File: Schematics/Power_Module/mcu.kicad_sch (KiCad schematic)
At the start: 38 parts, among them J5 USB_C_Female_USB2_Small, J6 SWD_B, J7 Stack Male Edge Connector, SW1 SW_STM_RESET, SW2 SW_STM_BOOT_MODE, U13 CP2102N-A02-GQFN20R, U14 STM32F103CBT6, U15 ISO1044BDR, U16 W25Q128JVS, Y1 X322516MMB4SI

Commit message: confirm layout, confirm everything fits
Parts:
- added C49: 22uF, symbol Device:C
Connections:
- net +3V3 is gone; now on net 3.3V_MUX: C46.1, U15.1 (VCC1)
- net +5V is gone; now on net 5.0V_A: C47.1, U15.8 (VCC2)
- net 24V_MUX: now also C49.1
- net GND: now also C49.2

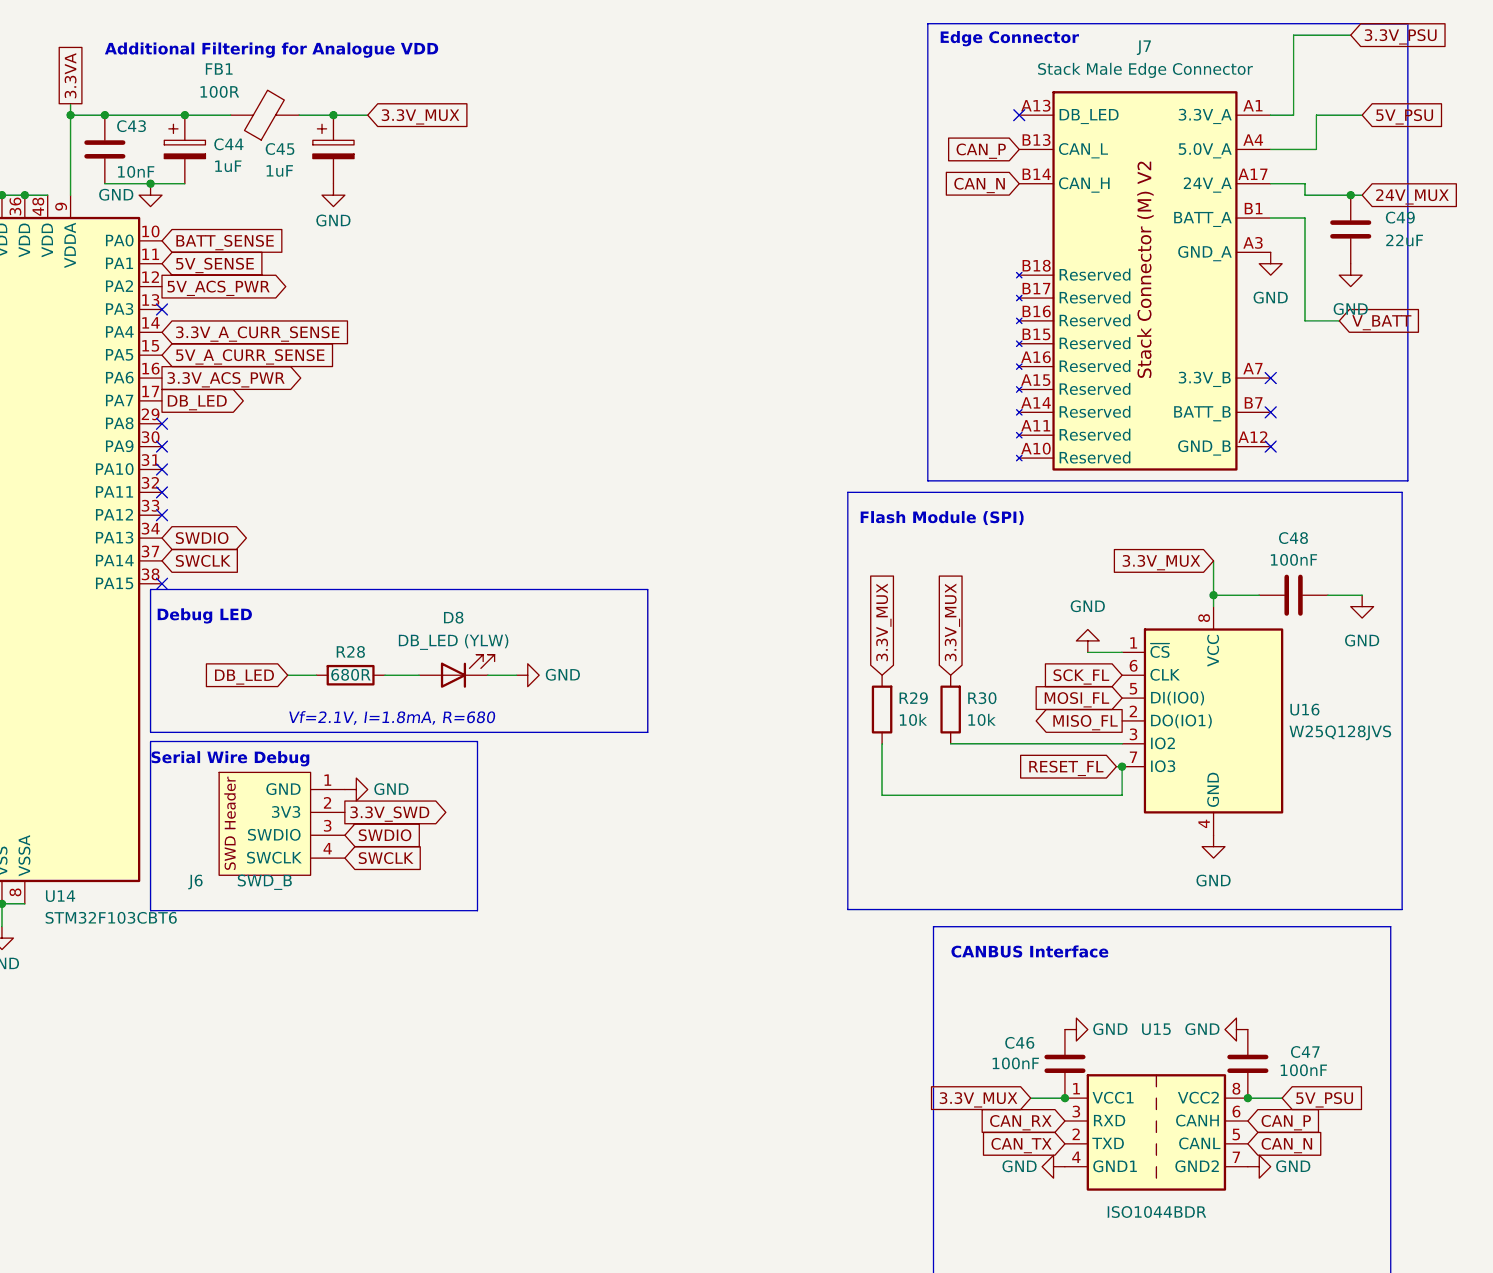
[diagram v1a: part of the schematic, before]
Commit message: completed all power traces, finalizing signal traces
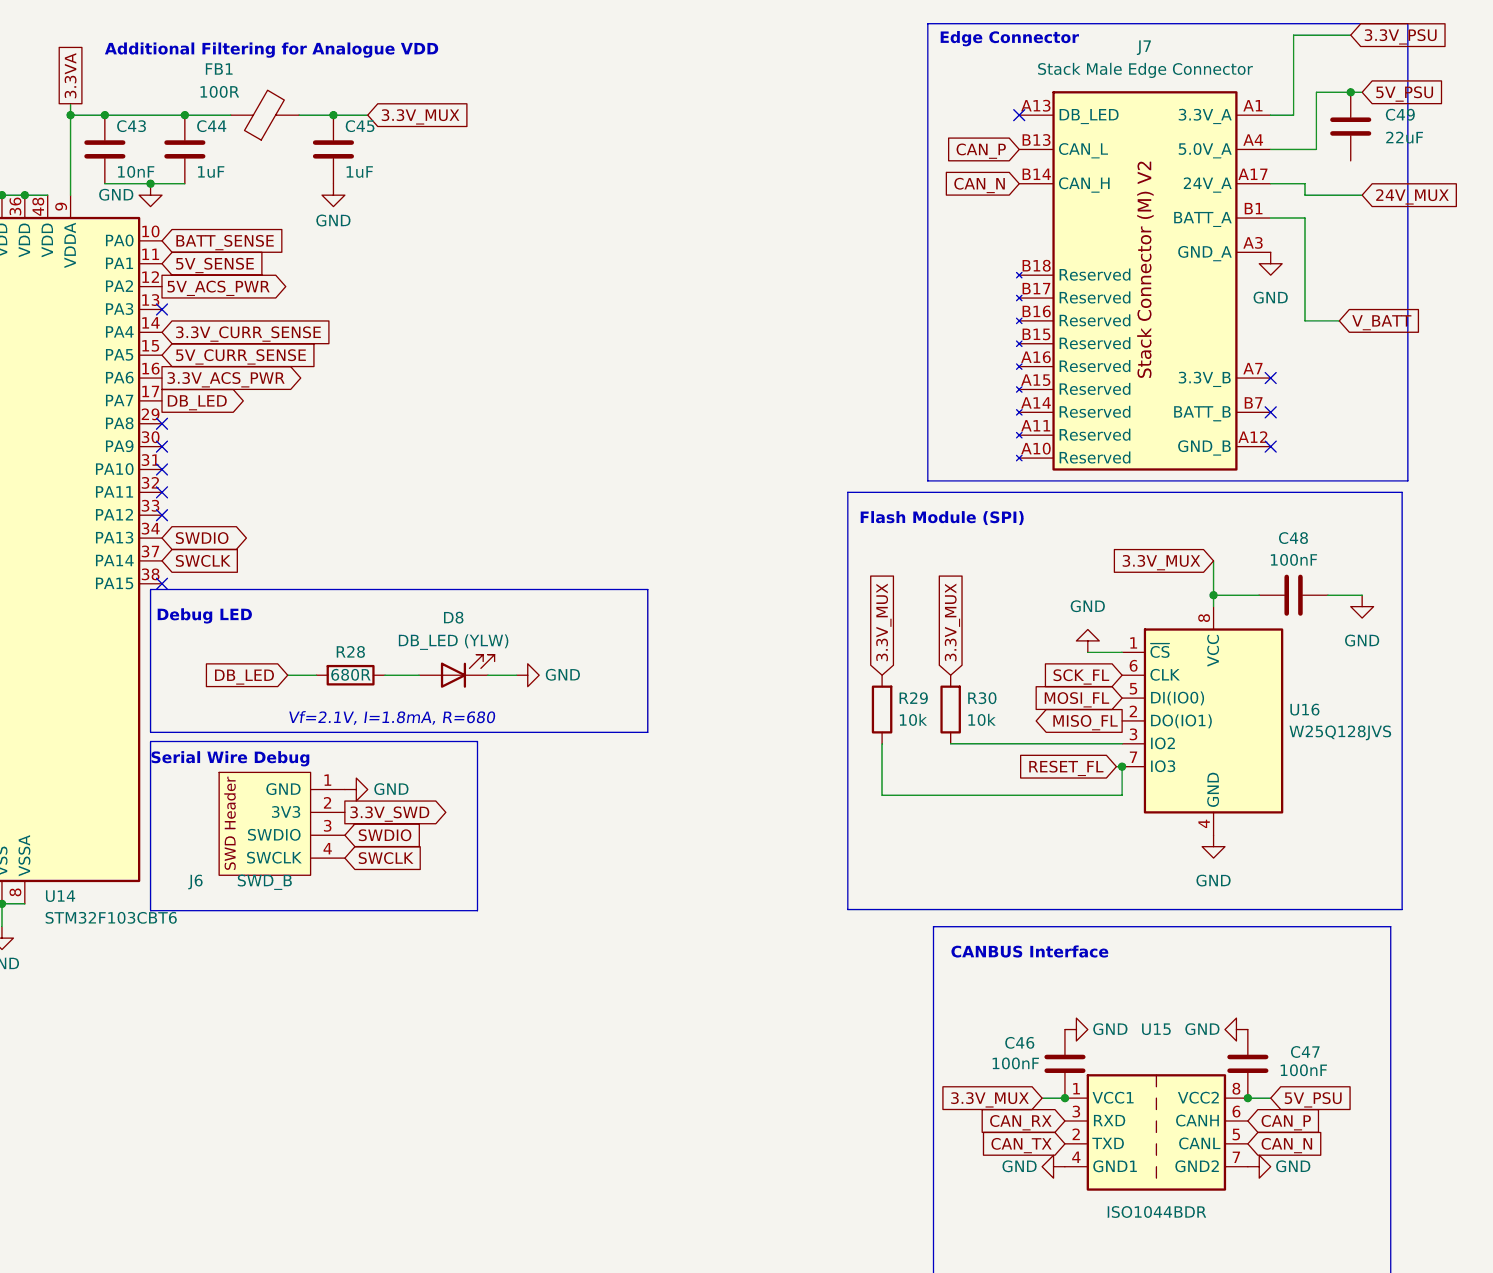
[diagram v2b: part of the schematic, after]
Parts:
- removed C44, C45: 1uF, Capacitor_SMD:C_0805_2012Metric, symbol Device:C_Polarized
- added C44, C45: 1uF, Capacitor_SMD:C_0603_1608Metric, symbol Device:C
- FB1: footprint Resistor_SMD:R_0805_2012Metric -> Inductor_SMD:L_0603_1608Metric; JLCPCB C1015 -> C1002
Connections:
- net 24V_MUX: no longer C49.1
- net 3.3VA: now also C44.1
- net 3.3V_MUX: now also C45.1
- net 5.0V_A: now also C49.1
- net GND: now also C44.2, C45.2; no longer C49.2
- net 3.3V_A_CURR_SENSE renamed 3.3V_CURR_SENSE
- net 5V_A_CURR_SENSE renamed 5V_CURR_SENSE

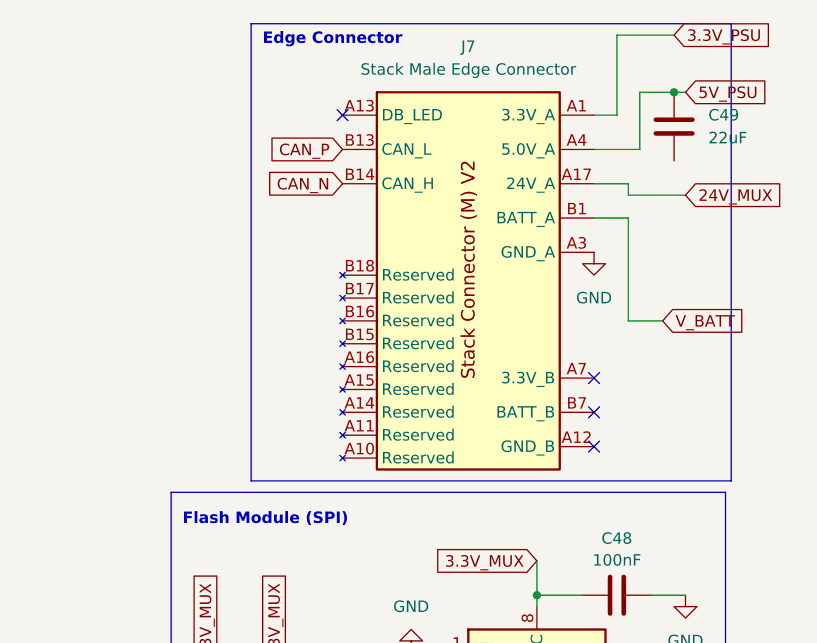
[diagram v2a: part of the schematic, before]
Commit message: continuing to finish signal traces, added extra decouplping caps near PCIE
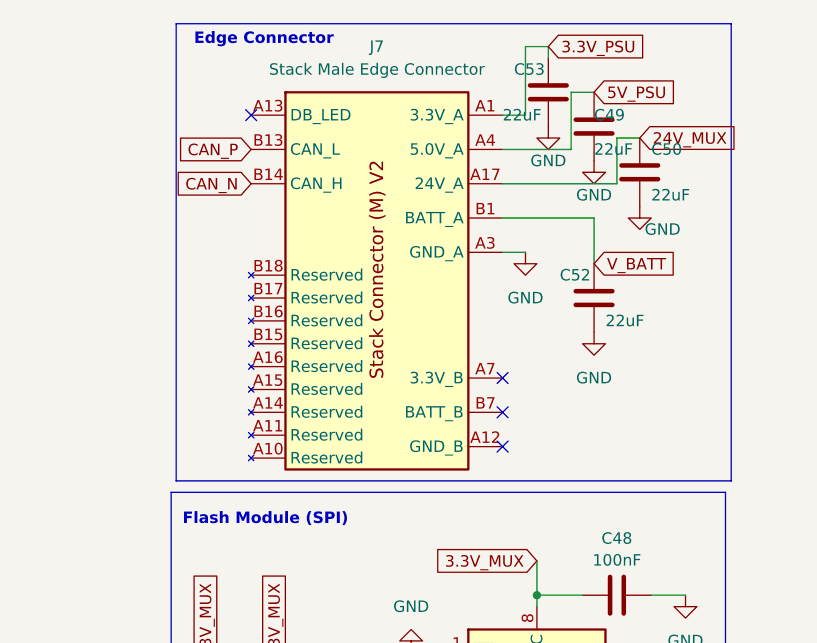
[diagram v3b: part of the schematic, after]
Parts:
- added C50, C52, C53: 22uF, Capacitor_SMD:C_1206_3216Metric, symbol Device:C
- C49: footprint (none) -> Capacitor_SMD:C_1206_3216Metric; Digikey (none) -> 445-8045-1-ND
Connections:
- net 24V_MUX: now also C50.1
- net 3.3V_PSU: now also C53.1
- net GND: now also C49.2, C50.2, C52.2, C53.2
- net V_BATT: now also C52.1
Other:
- moved on the sheet: J7

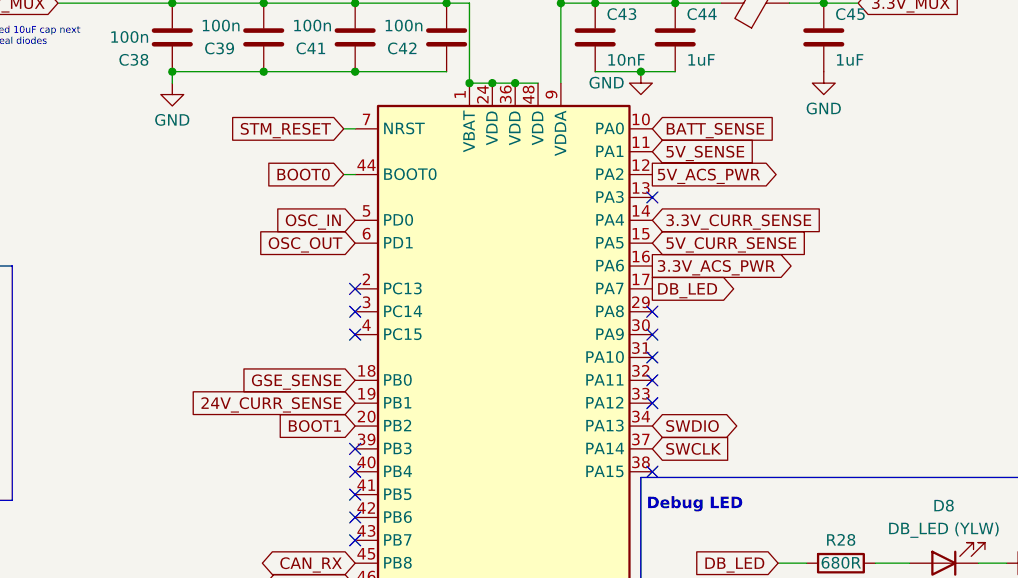
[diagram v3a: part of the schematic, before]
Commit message: finished all traces, confirmed major DRC errors  - need to fix silkscreen  - review needed and LCSC verification
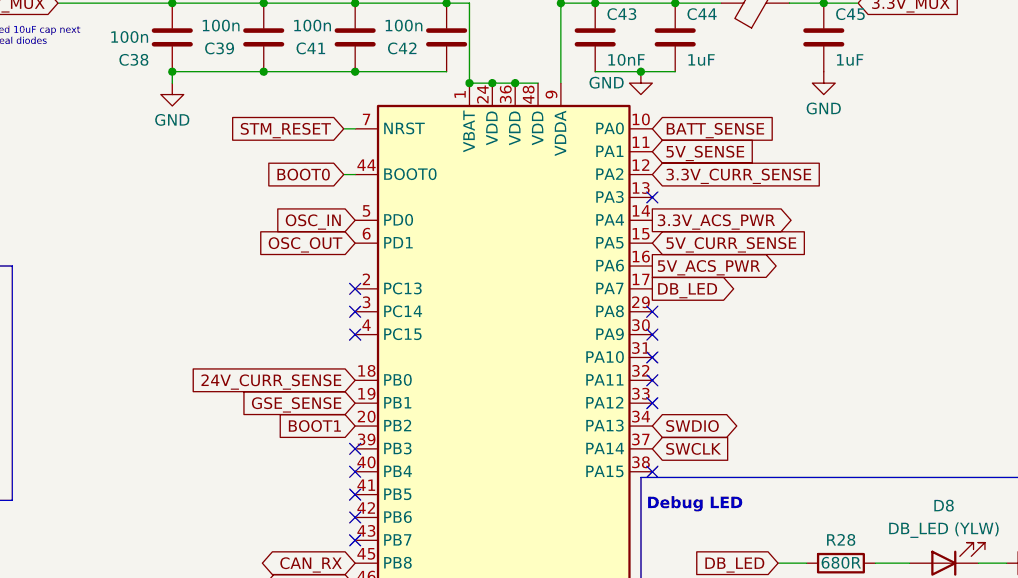
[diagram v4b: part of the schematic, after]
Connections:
- net 24V_CURR_SENSE: now also U14.18 (PB0); no longer U14.19 (PB1)
- net 3.3V_ACS_PWR: now also U14.14 (PA4); no longer U14.16 (PA6)
- net 3.3V_CURR_SENSE: now also U14.12 (PA2); no longer U14.14 (PA4)
- net 5V_ACS_PWR: now also U14.16 (PA6); no longer U14.12 (PA2)
- net GSE_SENSE: now also U14.19 (PB1); no longer U14.18 (PB0)
